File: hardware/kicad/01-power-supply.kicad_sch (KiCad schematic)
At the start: 29 parts, among them J1 USB_C, J3 JST PH 2-pin, Q1 SI2301CDS, U2 IP5306, U3 SY8089AAAC, U4 USBLC6-2SC6

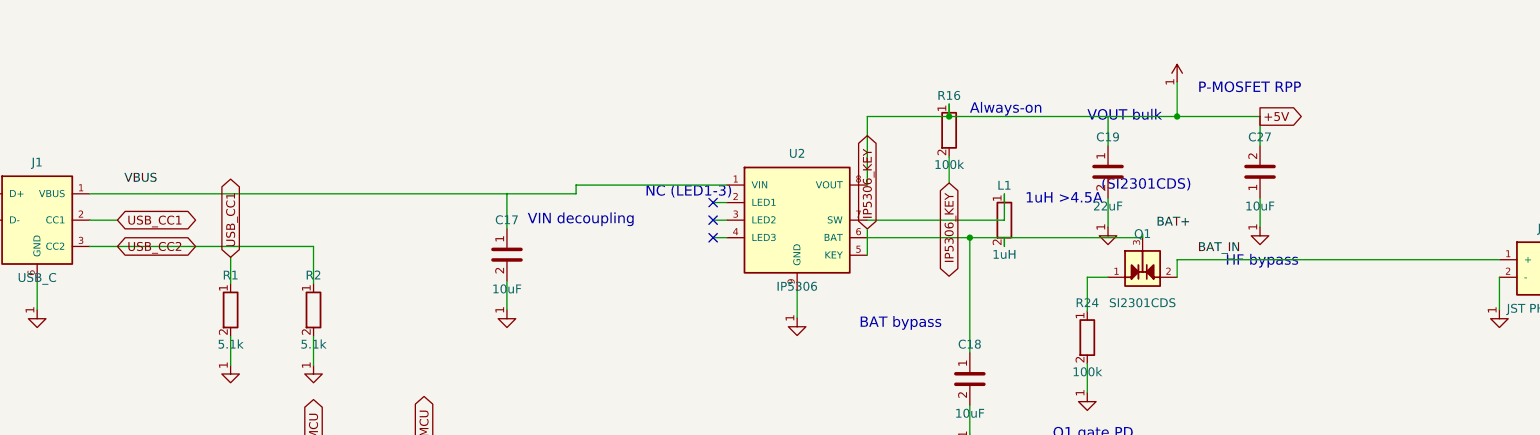
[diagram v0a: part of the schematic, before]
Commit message: triage: close the netlist disputes Phase 0 exposed — 29 down to 5
The plan forbids building the bench on a netlist in dispute, so the classes
scripts/vbench/netlist.py reported were worked through before Phase 1 opens.
Two of them were a fault in the detector, which is the more useful half.

D3 was a false-alarm class (17 -> 0). It reported every pad the schematic
translation table does not list and called them "compared by nothing". All
seventeen are declared in hardware/datasheet_specs.py, where
verify_datasheet_nets compares each against an expected net — 267 checks,
all passing. The four most suspicious readings dissolved on inspection:
U6.8/U6.9 on the SD data lines and SW_PWR.4b/4d on BTN_SELECT are
deliberate same-net assignments with a written safety analysis at
routing.py:6055-6085, protecting against real trace-through-pad shorts and
guarded by a hard gate. A check that fires on all seventeen discriminates
nothing, so D3 now fires only for a pad in NEITHER source — empty today,
and test_vbench injects one to prove the class still works, then requires
it to fall silent when the datasheet entry comes back.

Two of those entries were a real defect, in the table rather than the
board. _J1_MAP claimed "3,5,8 = SBU / unused, no net" and sent D+ to pad 6
and D- to pad 7 alone. The SBU pins are 3 and 9; pads 5 and 8 are the
flipped-orientation half of the pair and carry USB_D-/USB_D+, which
datasheet_specs.py::J1 states pad by pad citing USB-C r2.1 4.2. Two of the
four data pads were compared by nothing. T4 now compares all four.

The supply-rail stubs were the serious find. BAT+ had one node on the
schematic (SW_PWR.1) and VBUS had one (U4.5), because three local labels in
the Power Supply sheet sat 1.5-2 mm off the wires they name: VBUS at
vbus_y - 2, BAT+ at bat_y - 2, BAT_IN at jst_plus_y - 1.5. A label that
misses its wire leaves the wire unnamed, and KiCad drops unnamed nets from
the export — so the pins on them do not appear with a wrong net, they do
not ap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
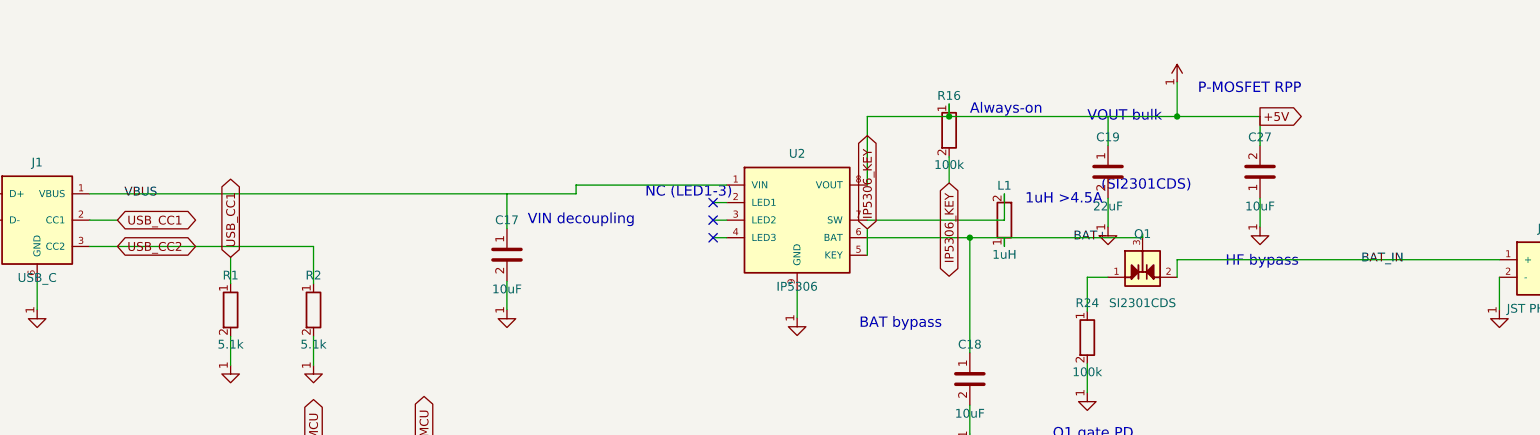
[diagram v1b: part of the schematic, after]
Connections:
- net BAT+: now also C18.1, L1.1, Q1.3, U2.6 (BAT)
- net BAT_IN: now also J3.1 (+), Q1.2
- net VBUS: now also C17.1, J1.1 (VBUS), U2.1 (VIN)
- net at U2.7 (SW): now also L1.2; no longer L1.1
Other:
- moved on the sheet: L1
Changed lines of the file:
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@@
   (symbol (lib_id "IP5306") (at 160 85 0) (unit 1) (exclude_from_sim no) (in_bom yes) (on_board yes) (dnp no) (property "Reference" "U2" (at 160 75.38 0) (effects (font (size 1.27 1.27)))) (property "Value" "IP5306" (at 160 94.62 0) (effects (font (size 1.27 1.27)))) (pin "1") (pin "2") (pin "3") (pin "4") (pin "5") (pin "6") (pin "7") (pin "8") (pin "9") (instances (project "esp32-emu-turbo" (path "/00000002-cafe-4000-8000-000000000002" (reference "U2") (unit 1)))))
   (wire (pts (xy 57.62 81.19) (xy 118 81.19)) (stroke (width 0) (type default)))
-  (label "VBUS" (at 62.62 79.19 0) (effects (font (size 1.27 1.27))))
+  (label "VBUS" (at 62.62 81.19 0) (effects (font (size 1.27 1.27))))
   (wire (pts (xy 118 81.19) (xy 118 86.19)) (stroke (width 0) (type default)))
   (symbol (lib_id "C") (at 118 90 0) (unit 1) (exclude_from_sim no) (in_bom yes) (on_board yes) (dnp no) (property "Reference" "C17" (at 118 85.0 0) (effects (font (size 1.27 1.27)))) (property "Value" "10uF" (at 118 95.0 0) (effects (font (size 1.27 1.27)))) (pin "1") (pin "2") (instances (project "esp32-emu-turbo" (path "/00000002-cafe-4000-8000-000000000002" (reference "C17") (unit 1)))))
@@
   (symbol (lib_id "GND") (at 160 99.16 0) (unit 1) (exclude_from_sim no) (in_bom no) (on_board no) (dnp no) (property "Reference" "#PWR006" (at 160 97.16 0) (effects (font (size 1.27 1.27)) hide)) (property "Value" "GND" (at 160 101.16 0) (effects (font (size 1.27 1.27)) hide)) (pin "1") (instances (project "esp32-emu-turbo" (path "/00000002-cafe-4000-8000-000000000002" (reference "#PWR006") (unit 1)))))
   (wire (pts (xy 160 95.16) (xy 160 99.16)) (stroke (width 0) (type default)))
-  (symbol (lib_id "L") (at 190 85 0) (unit 1) (exclude_from_sim no) (in_bom yes) (on_board yes) (dnp no) (property "Reference" "L1" (at 190 80.0 0) (effects (font (size 1.27 1.27)))) (property "Value" "1uH" (at 190 90.0 0) (effects (font (size 1.27 1.27)))) (pin "1") (pin "2") (instances (project "esp32-emu-turbo" (path "/00000002-cafe-4000-8000-000000000002" (reference "L1") (unit 1)))))
+  (symbol (lib_id "L") (at 190 85 180) (unit 1) (exclude_from_sim no) (in_bom yes) (on_board yes) (dnp no) (property "Reference" "L1" (at 190 80.0 0) (effects (font (size 1.27 1.27)))) (property "Value" "1uH" (at 190 90.0 0) (effects (font (size 1.27 1.27)))) (pin "1") (pin "2") (instances (project "esp32-emu-turbo" (path "/00000002-cafe-4000-8000-000000000002" (reference "L1") (unit 1)))))
   (text "1uH >4.5A" (at 193 82 0) (effects (font (size 1.5 1.5)) (justify left)))
   (wire (pts (xy 170.16 87.54) (xy 190 87.54)) (stroke (width 0) (type default)))
@@
   (junction (at 185 87.54) (diameter 0) (color 0 0 0 0))
   (wire (pts (xy 210 87.54) (xy 210 87)) (stroke (width 0) (type default)))
-  (label "BAT+" (at 212 85.54 0) (effects (font (size 1.27 1.27))))
+  (label "BAT+" (at 200 87.54 0) (effects (font (size 1.27 1.27))))
   (wire (pts (xy 215 93.27) (xy 215 90.73)) (stroke (width 0) (type default)))
   (wire (pts (xy 215 90.73) (xy 261.65 90.73)) (stroke (width 0) (type default)))
-  (label "BAT_IN" (at 218 89.23 0) (effects (font (size 1.27 1.27))))
+  (label "BAT_IN" (at 241.64999999999998 90.73 0) (effects (font (size 1.27 1.27))))
   (symbol (lib_id "R") (at 202 102 0) (unit 1) (exclude_from_sim no) (in_bom yes) (on_board yes) (dnp no) (property "Reference" "R24" (at 202 97.0 0) (effects (font (size 1.27 1.27)))) (property "Value" "100k" (at 202 107.0 0) (effects (font (size 1.27 1.27)))) (pin "1") (pin "2") (instances (project "esp32-emu-turbo" (path "/00000002-cafe-4000-8000-000000000002" (reference "R24") (unit 1)))))
   (text "Q1 gate PD" (at 197 116 0) (effects (font (size 1.5 1.5)) (justify left)))

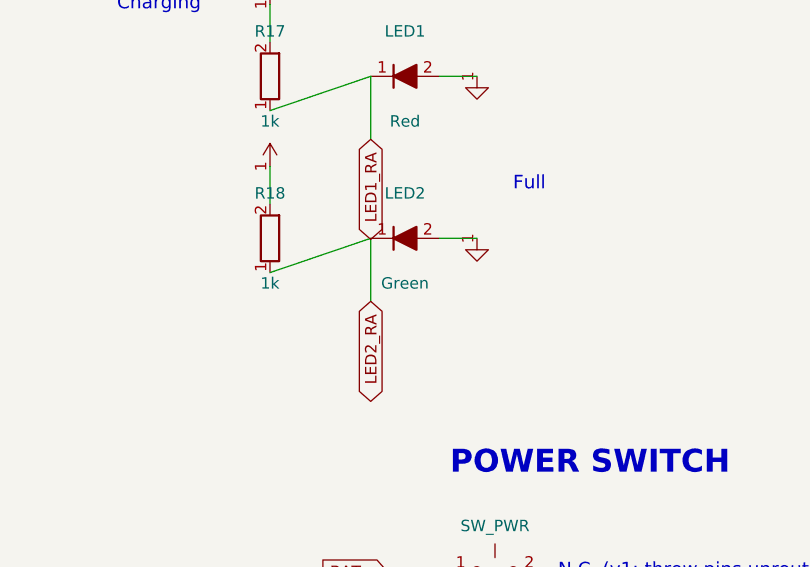
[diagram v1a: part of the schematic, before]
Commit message: H6 closed by the datasheets: nothing was inverted — the two LED vendors number their pins oppositely
The question H6 said only a magnifying glass could settle is settled from
documents. Both LED datasheets are now IN the repo, and they dissolve the
premise rather than pick a side:

  LED1 C84256   NationStar NCD0805R1: mark = cathode = pin 1.
  LED2 C19171391 YONGYUTAI YLED0805R: p.1 draws pin 1 with a "+" — the
                ANODE — and puts the green mark at pin 2, the cathode.

"C19171391's pad numbering is inverted relative to its cathode mark" was
never a fact about the part; it was the extractors' assumption that pin 1 =
cathode for every LED, applied to a vendor that numbers the other way. The
EasyEDA footprint follows YONGYUTAI exactly (cache re-read independently:
pad 1 x=+1.05, silk feature mean x=-0.38 — opposite ends, as intended), and
the rival "machine aligns by the 3D model" frame collapses because model
patch and silk sit at the same pad-2/cathode end: the frames only ever
disagreed about labels, not placement.

From there the override is arithmetic. Board copper (verified): both LED
footprints identical, pad 1 = GND needs cathode, pad 2 = LED_RA -> R ->
+3V3 needs anode. Identical placements + opposite pin-1 conventions force a
180 deg CPL delta, and the shipped CPL is exactly LED1=0/LED2=180. The
pad-number frame is hardware-anchored by U2 (protos #1/#2). Prediction for
proto #1 (pre-fix CPL, LED2 at 0): reversed, dark whenever powered — and
NOT charge-confounded, because U2's LED pins 2-4 are NC and both LEDs are
plain +3V3 power indicators. The old "don't use 'does it light'" advice
was itself wrong.

Two mislabels found on the way, both corrected end to end:

  * C19171391 is RED (615-630 nm, YLED0805R — the R is in the MPN). BOM,
    CPL Val, schematic value, board.py comment, datasheet_specs, two gates'
    descriptions, both doc tables, and the datasheet FILENAME all said
    green. The repo's LED2_Green-...pdf was byte-identical (same md5)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
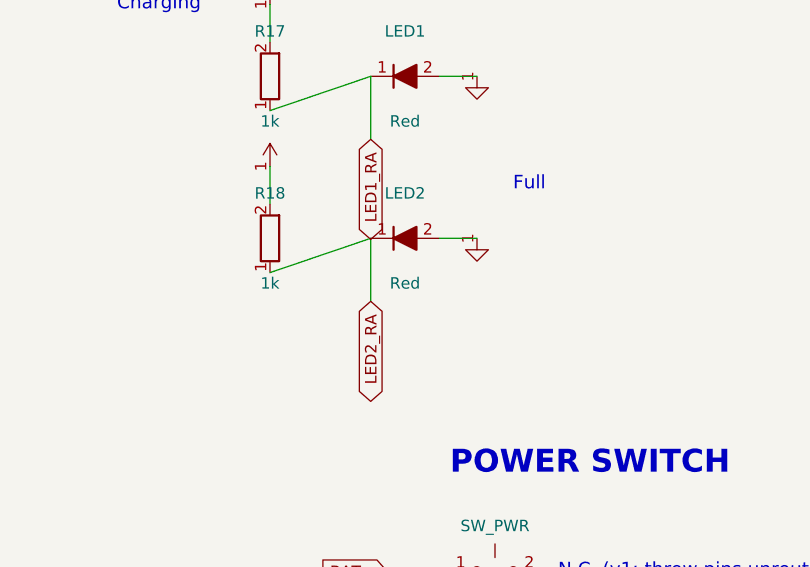
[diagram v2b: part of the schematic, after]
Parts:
- LED2: value Green -> Red
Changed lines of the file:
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@@
   (text "Charging" (at 243 137 0) (effects (font (size 1.5 1.5)) (justify left)))
   (symbol (lib_id "R") (at 260 163 180) (unit 1) (exclude_from_sim no) (in_bom yes) (on_board yes) (dnp no) (property "Reference" "R18" (at 260 158.0 0) (effects (font (size 1.27 1.27)))) (property "Value" "1k" (at 260 168.0 0) (effects (font (size 1.27 1.27)))) (pin "1") (pin "2") (instances (project "esp32-emu-turbo" (path "/00000002-cafe-4000-8000-000000000002" (reference "R18") (unit 1)))))
-  (symbol (lib_id "LED") (at 275 163 0) (unit 1) (exclude_from_sim no) (in_bom yes) (on_board yes) (dnp no) (property "Reference" "LED2" (at 275 158.0 0) (effects (font (size 1.27 1.27)))) (property "Value" "Green" (at 275 168.0 0) (effects (font (size 1.27 1.27)))) (pin "1") (pin "2") (instances (project "esp32-emu-turbo" (path "/00000002-cafe-4000-8000-000000000002" (reference "LED2") (unit 1)))))
+  (symbol (lib_id "LED") (at 275 163 0) (unit 1) (exclude_from_sim no) (in_bom yes) (on_board yes) (dnp no) (property "Reference" "LED2" (at 275 158.0 0) (effects (font (size 1.27 1.27)))) (property "Value" "Red" (at 275 168.0 0) (effects (font (size 1.27 1.27)))) (pin "1") (pin "2") (instances (project "esp32-emu-turbo" (path "/00000002-cafe-4000-8000-000000000002" (reference "LED2") (unit 1)))))
   (symbol (lib_id "+3V3") (at 260 155 0) (unit 1) (exclude_from_sim no) (in_bom no) (on_board no) (dnp no) (property "Reference" "#PWR024" (at 260 153 0) (effects (font (size 1.27 1.27)) hide)) (property "Value" "+3V3" (at 260 157 0) (effects (font (size 1.27 1.27)) hide)) (pin "1") (instances (project "esp32-emu-turbo" (path "/00000002-cafe-4000-8000-000000000002" (reference "#PWR024") (unit 1)))))
   (wire (pts (xy 260 155) (xy 260 159.19)) (stroke (width 0) (type default)))

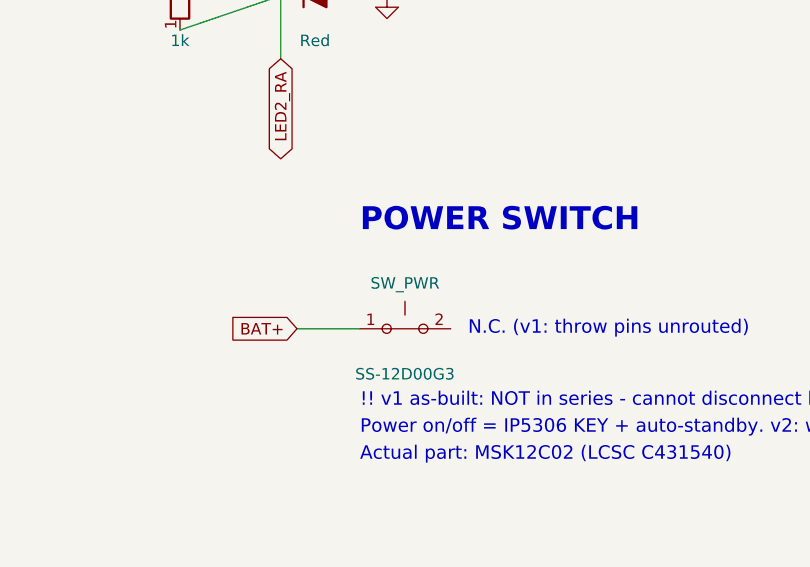
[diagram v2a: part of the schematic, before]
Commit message: refactor(refs): rename SW_PWR/SW_BOOT/SW_RST to IPC SW16/SW14/SW15
KiBot (>= 1.6.5, upstream #604, wontfix) hard-rejects schematic
references that are not PREFIX+NUMBER, which blocked its schematic
phase (ERC + BOM cross-check) forever. User-approved rename across the
whole chain in one commit: generators (PCB + schematics), datasheet
specs, verify scripts, vbench (scenarios, netlist, sim headers), skills,
issues, docs, website — plus regenerated .kicad_pcb/.kicad_sch, BOM,
CPL, d356, gerbers, renders, iBOM, Net Explorer, and release_jlcpcb/
fully synced. SW13 was already the MENU button, so the switches take
SW14 (BOOT), SW15 (RST), SW16 (PWR slide). Both datasheet PDFs
(hardware/datasheets/ + website/static/datasheets/) renamed to match.

external-dfm.sh: single full KiBot run restored (-e included) with a
regression guard on "Malformed component reference"; CI workflow
extended the same way. Three latent script bugs fixed while unblocking
paths that had never executed: bare failing python under set -e killed
the script before the summary; grep|head SIGPIPE (141) under pipefail;
and the ERC JSON parser read top-level violations[] (the DRC shape)
while ERC nests them under sheets[] — a false "0 errors". KiBot BOM
CSV parsing now handles KiBot 1.9's space-separated refs + stats block.

First-ever ERC run found 4 error-level schematic-DRAWING bugs (dangling
GND in controls, dangling BTN_LEFT label in mcu, +3V3 with no power
driver x2) — pre-existing, copper unaffected, recorded in memory as
owned follow-up work for generate_schematics. make external-dfm is red
on them honestly.

Tests: verify-all 77/77, gate-coverage 9/9 fault classes caught,
verify-fast 124/124, verify-dfa 9/9, firmware-sync-check PASS,
KiBot DRC 0 errors, BOM cross-ref 81/81 assembled parts matched,
website-build green.

Co-Authored-By: Claude Fable 5 <noreply@anthropic.com>
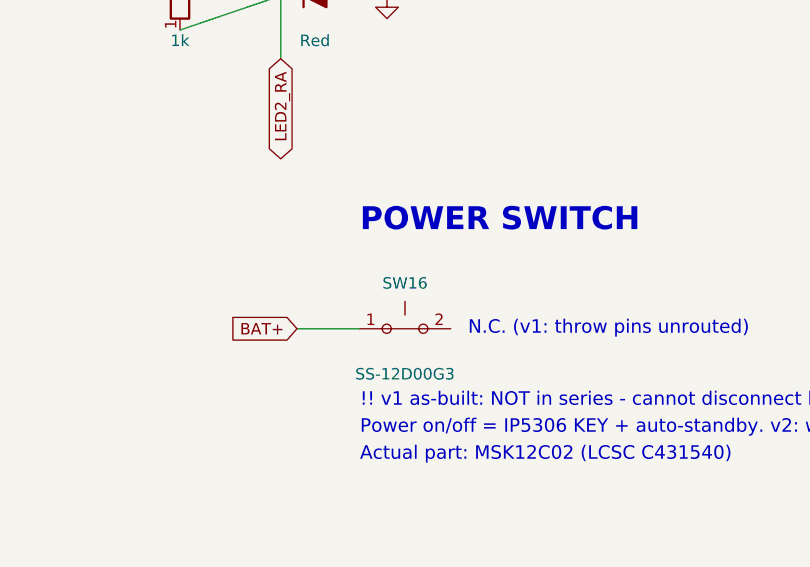
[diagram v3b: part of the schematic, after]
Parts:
- renumbered SW_PWR to SW16
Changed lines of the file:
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@@
   (text "C29 = datasheet feed-forward cap (load transient)" (at 195 269 0) (effects (font (size 1.8 1.8)) (justify left)))
   (text "POWER SWITCH" (at 280 188 0) (effects (font (size 2.54 2.54) bold) (justify left)))
-  (symbol (lib_id "SW_Push") (at 285 200 0) (unit 1) (exclude_from_sim no) (in_bom yes) (on_board yes) (dnp no) (property "Reference" "SW_PWR" (at 285 194.952 0) (effects (font (size 1.27 1.27)))) (property "Value" "SS-12D00G3" (at 285 205.048 0) (effects (font (size 1.27 1.27)))) (pin "1") (pin "2") (instances (project "esp32-emu-turbo" (path "/00000002-cafe-4000-8000-000000000002" (reference "SW_PWR") (unit 1)))))
+  (symbol (lib_id "SW_Push") (at 285 200 0) (unit 1) (exclude_from_sim no) (in_bom yes) (on_board yes) (dnp no) (property "Reference" "SW16" (at 285 194.952 0) (effects (font (size 1.27 1.27)))) (property "Value" "SS-12D00G3" (at 285 205.048 0) (effects (font (size 1.27 1.27)))) (pin "1") (pin "2") (instances (project "esp32-emu-turbo" (path "/00000002-cafe-4000-8000-000000000002" (reference "SW16") (unit 1)))))
   (text "Actual part: MSK12C02 (LCSC C431540)" (at 280 214 0) (effects (font (size 1.5 1.5)) (justify left)))
   (global_label "BAT+" (shape input) (at 273 200 180) (effects (font (size 1.27 1.27))) (property "Intersheetrefs" "" (at 0 0 0) (effects (font (size 1.27 1.27)) hide)))
